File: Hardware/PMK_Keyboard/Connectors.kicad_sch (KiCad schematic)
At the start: 3 parts, among them J101 USB_C_Receptacle_USB2.0

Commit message: Worked on hierachic page again
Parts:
- renumbered J101 to J?
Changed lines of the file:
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@@
+    (stroke (width 0) (type default) (color 0 0 0 0))
+  )
+  (wire (pts (xy 266.7 33.02) (xy 269.24 33.02))
     (stroke (width 0) (type default) (color 0 0 0 0))
   )
@@
     (stroke (width 0) (type default) (color 0 0 0 0))
   )
+  (wire (pts (xy 269.24 36.83) (xy 264.16 36.83))
+    (stroke (width 0) (type default) (color 0 0 0 0))
+  )
   (wire (pts (xy 124.46 93.98) (xy 154.94 93.98))
     (stroke (width 0) (type default) (color 0 0 0 0))
@@
     (stroke (width 0) (type default) (color 0 0 0 0))
   )
+  (wire (pts (xy 264.16 24.13) (xy 264.16 25.4))
+    (stroke (width 0) (type default) (color 0 0 0 0))
+  )
+  (wire (pts (xy 264.16 36.83) (xy 264.16 38.1))
+    (stroke (width 0) (type default) (color 0 0 0 0))
+  )
   (wire (pts (xy 127 106.68) (xy 127 109.22))
     (stroke (width 0) (type default) (color 0 0 0 0))
@@
     (stroke (width 0) (type default) (color 0 0 0 0))
   )
+  (wire (pts (xy 266.7 29.21) (xy 269.24 29.21))
+    (stroke (width 0) (type default) (color 0 0 0 0))
+  )
   (wire (pts (xy 127 104.14) (xy 127 101.6))
     (stroke (width 0) (type default) (color 0 0 0 0))
@@
   )
   (wire (pts (xy 127 86.36) (xy 127 88.9))
+    (stroke (width 0) (type default) (color 0 0 0 0))
+  )
+  (wire (pts (xy 264.16 25.4) (xy 269.24 25.4))
     (stroke (width 0) (type default) (color 0 0 0 0))
   )
@@
     (effects (font (size 1.27 1.27)) (justify left bottom))
   )
-  (global_label "D-" (shape input) (at 129.54 101.6 0) (fields_autoplaced)
+  (global_label "D+" (shape bidirectional) (at 266.7 33.02 180) (fields_autoplaced)
+    (effects (font (size 1.27 1.27)) (justify right))
+    (property "Intersheet References" "${INTERSHEET_REFS}" (id 0) (at 261.4445 32.9406 0)
+      (effects (font (size 1.27 1.27)) (justify right) hide)
+    )
+  )
+  (global_label "D-" (shape bidirectional) (at 129.54 101.6 0) (fields_autoplaced)
     (effects (font (size 1.27 1.27)) (justify left))
     (property "Intersheet References" "${INTERSHEET_REFS}" (id 0) (at 134.7955 101.5206 0)
@@
     )
   )
-  (global_label "D+" (shape input) (at 129.54 106.68 0) (fields_autoplaced)
+  (global_label "D+" (shape bidirectional) (at 129.54 106.68 0) (fields_autoplaced)
     (effects (font (size 1.27 1.27)) (justify left))
     (property "Intersheet References" "${INTERSHEET_REFS}" (id 0) (at 134.7955 106.6006 0)
@@
     )
   )
+  (global_label "D-" (shape bidirectional) (at 266.7 29.21 180) (fields_autoplaced)
+    (effects (font (size 1.27 1.27)) (justify right))
+    (property "Intersheet References" "${INTERSHEET_REFS}" (id 0) (at 261.4445 29.2894 0)
+      (effects (font (size 1.27 1.27)) (justify right) hide)
+    )
+  )
+  (hierarchical_label "D+" (shape bidirectional) (at 269.24 33.02 0)
+    (effects (font (size 1.27 1.27)) (justify left))
+  )
+  (hierarchical_label "GND" (shape passive) (at 269.24 36.83 0)
+    (effects (font (size 1.27 1.27)) (justify left))
+  )
+  (hierarchical_label "VBUS" (shape output) (at 269.24 25.4 0)
+    (effects (font (size 1.27 1.27)) (justify left))
+  )
+  (hierarchical_label "D-" (shape bidirectional) (at 269.24 29.21 0)
+    (effects (font (size 1.27 1.27)) (justify left))
+  )
   (symbol (lib_id "Component lib:R") (at 144.78 99.06 0) (unit 1)
     (in_bom yes) (on_board yes) (fields_autoplaced)
@@
   (symbol (lib_id "power:GND") (at 101.6 129.54 0) (unit 1)
     (in_bom yes) (on_board yes) (fields_autoplaced)
-    (property "Reference" "#PWR084" (id 0) (at 101.6 135.89 0)
+    (property "Reference" "#PWR?" (id 0) (at 101.6 135.89 0)
       (effects (font (size 1.27 1.27)) hide)
     )
@@
   (symbol (lib_id "power:GND") (at 144.78 109.22 0) (unit 1)
     (in_bom yes) (on_board yes) (fields_autoplaced)
-    (property "Reference" "#PWR082" (id 0) (at 144.78 115.57 0)
+    (property "Reference" "#PWR?" (id 0) (at 144.78 115.57 0)
       (effects (font (size 1.27 1.27)) hide)
     )
@@
     (pin "1")
   )
+  (symbol (lib_id "power:VBUS") (at 264.16 24.13 0) (unit 1)
+    (in_bom yes) (on_board yes) (fields_autoplaced)
+    (property "Reference" "#PWR?" (id 0) (at 264.16 27.94 0)
+      (effects (font (size 1.27 1.27)) hide)
+    )
+    (property "Value" "VBUS" (id 1) (at 264.16 20.5542 0))
+    (property "Footprint" "" (id 2) (at 264.16 24.13 0)
+      (effects (font (size 1.27 1.27)) hide)
+    )
+    (property "Datasheet" "" (id 3) (at 264.16 24.13 0)
+      (effects (font (size 1.27 1.27)) hide)
+    )
+    (pin "1")
+  )
   (symbol (lib_id "power:GND") (at 109.22 129.54 0) (unit 1)
     (in_bom yes) (on_board yes) (fields_autoplaced)
-    (property "Reference" "#PWR085" (id 0) (at 109.22 135.89 0)
+    (property "Reference" "#PWR?" (id 0) (at 109.22 135.89 0)
       (effects (font (size 1.27 1.27)) hide)
     )
@@
   (symbol (lib_id "power:GND") (at 154.94 109.22 0) (unit 1)
     (in_bom yes) (on_board yes) (fields_autoplaced)
-    (property "Reference" "#PWR083" (id 0) (at 154.94 115.57 0)
+    (property "Reference" "#PWR?" (id 0) (at 154.94 115.57 0)
       (effects (font (size 1.27 1.27)) hide)
     )
@@
     (pin "2")
   )
+  (symbol (lib_id "power:GND") (at 264.16 38.1 0) (unit 1)
+    (in_bom yes) (on_board yes) (fields_autoplaced)
+    (property "Reference" "#PWR?" (id 0) (at 264.16 44.45 0)
+      (effects (font (size 1.27 1.27)) hide)
+    )
+    (property "Value" "GND" (id 1) (at 264.16 42.5434 0))
+    (property "Footprint" "" (id 2) (at 264.16 38.1 0)
+      (effects (font (size 1.27 1.27)) hide)
+    )
+    (property "Datasheet" "" (id 3) (at 264.16 38.1 0)
+      (effects (font (size 1.27 1.27)) hide)
+    )
+    (pin "1")
+  )
   (symbol (lib_id "power:VBUS") (at 127 86.36 0) (unit 1)
     (in_bom yes) (on_board yes) (fields_autoplaced)
-    (property "Reference" "#PWR081" (id 0) (at 127 90.17 0)
+    (property "Reference" "#PWR?" (id 0) (at 127 90.17 0)
       (effects (font (size 1.27 1.27)) hide)
     )
@@
   (symbol (lib_id "Connector:USB_C_Receptacle_USB2.0") (at 109.22 104.14 0) (unit 1)
     (in_bom yes) (on_board yes) (fields_autoplaced)
-    (property "Reference" "J101" (id 0) (at 109.22 82.6602 0))
+    (property "Reference" "J?" (id 0) (at 109.22 82.6602 0))
     (property "Value" "USB_C_Receptacle_USB2.0" (id 1) (at 109.22 85.1971 0))
     (property "Footprint" "" (id 2) (at 113.03 104.14 0)

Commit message: Worked on hierachic sheet
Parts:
- added J102: Conn_01x02_MountingPin, symbol Connector_Generic_MountingPin:Conn_01x02_MountingPin
- gave numbers to parts that had none: 1
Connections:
- net GND: now also J102.2 (Pin_2), J102.MP (MountPin)
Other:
- moved on the sheet: J101, R101, R102

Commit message: Again on hierachic sheet
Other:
- company: (none) -> PumaCorp
- title: (none) -> PMK_Keyboard
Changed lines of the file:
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@@
 (kicad_sch (version 20211123) (generator eeschema)
   (paper "A4")
+  (title_block
+    (title "PMK_Keyboard")
+    (date "2023-02-06")
+    (rev "HW00")
+    (company "PumaCorp")
+    (comment 1 "Design by: NdG")
+  )
   (junction (at 69.85 68.58) (diameter 0) (color 0 0 0 0)
   )

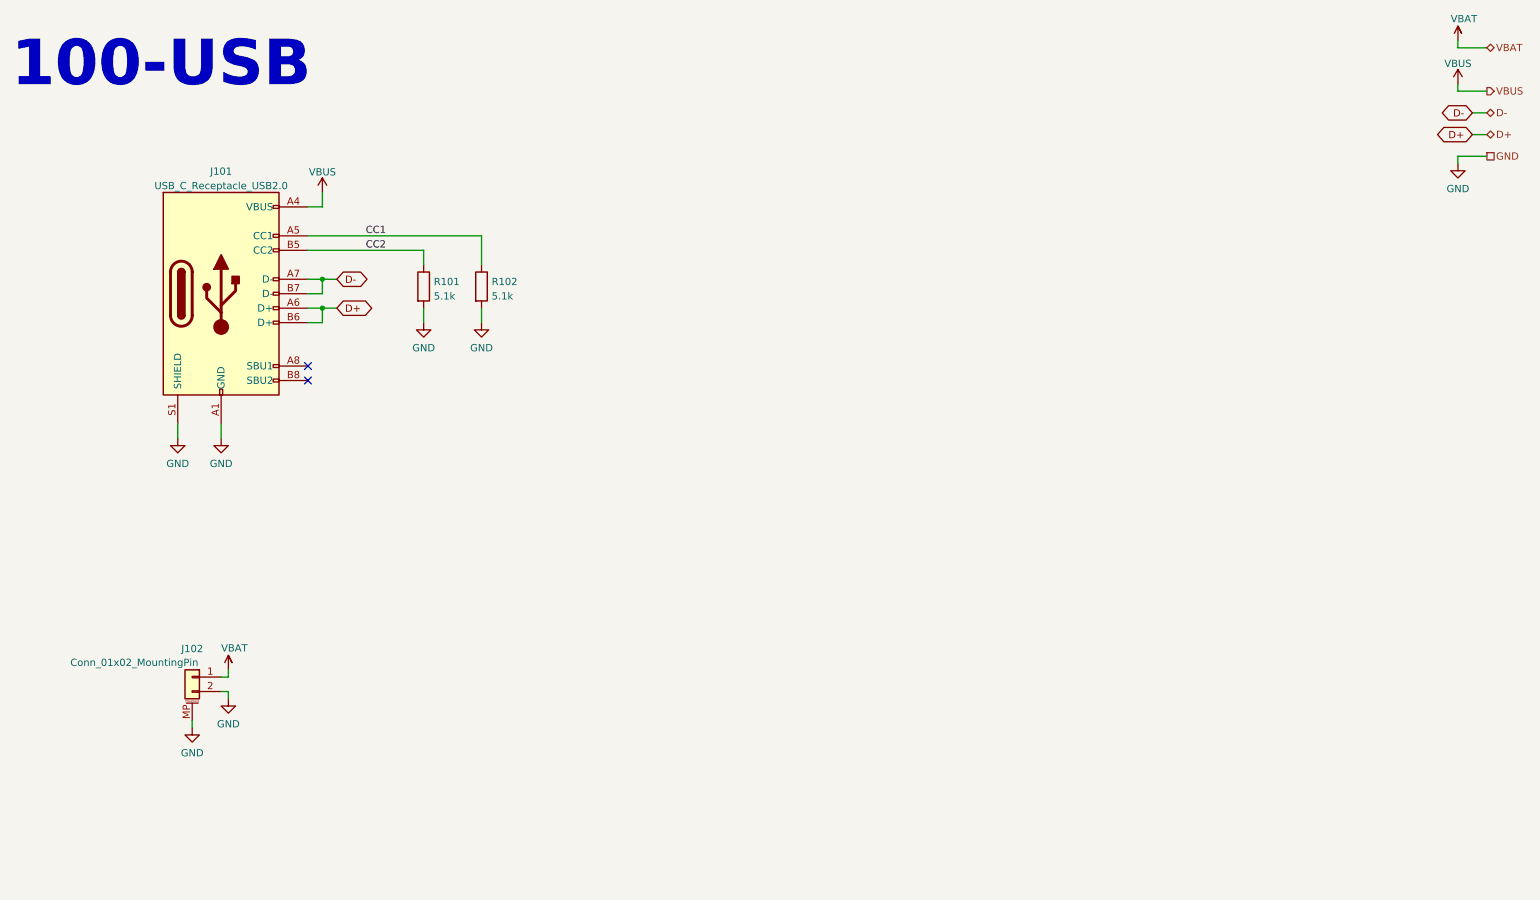
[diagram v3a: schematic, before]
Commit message: Schematic is done, only possible update is change of ESP pins
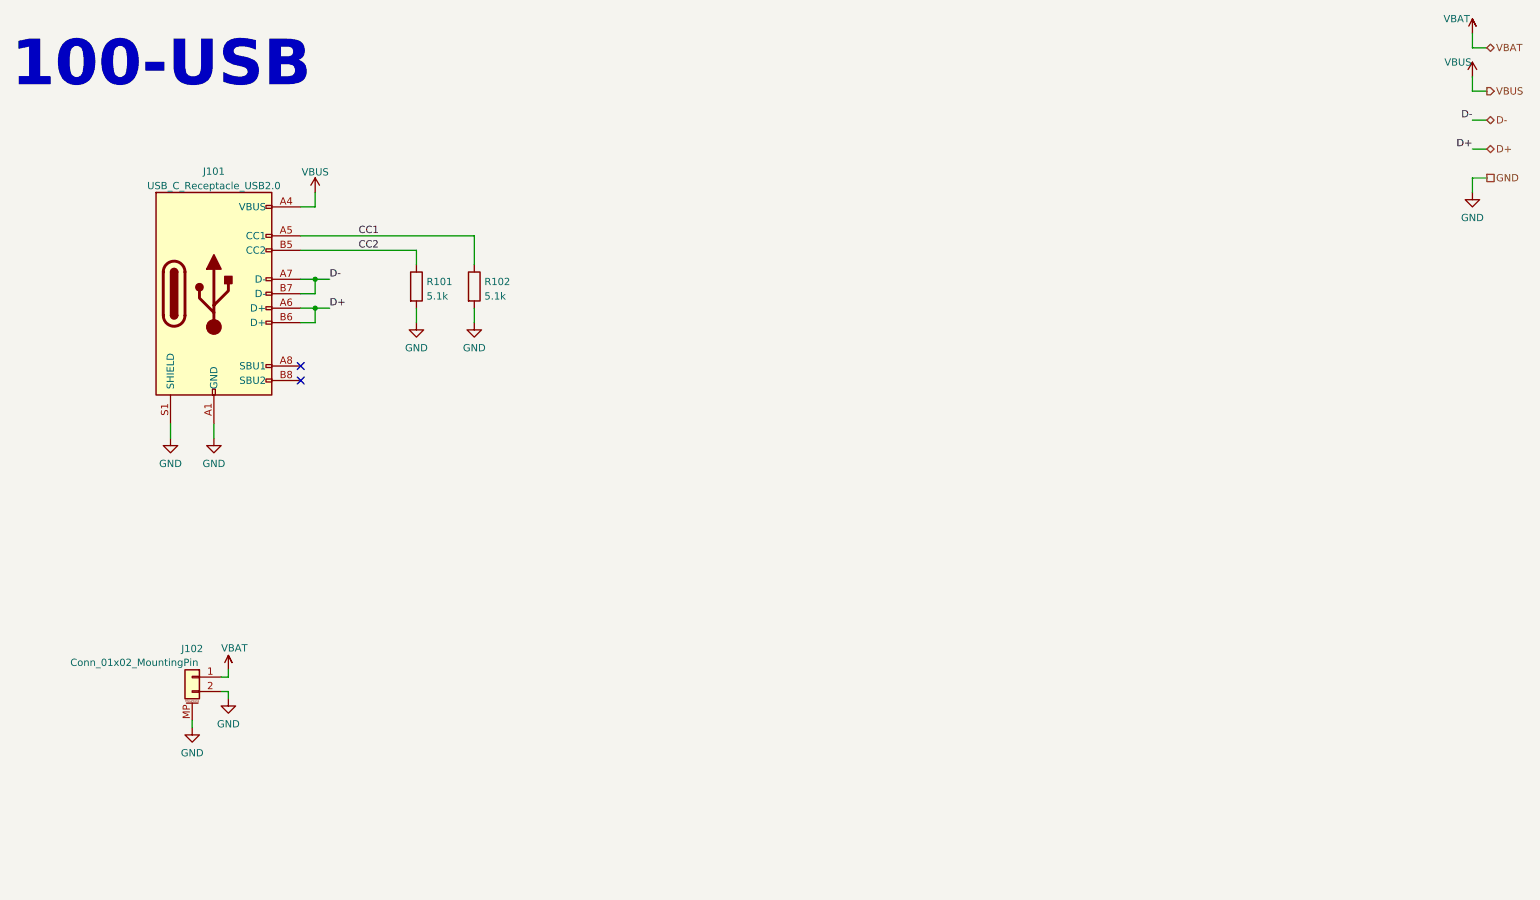
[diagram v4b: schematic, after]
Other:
- moved on the sheet: J101, R101, R102

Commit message: Routing is finally updated
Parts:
- J101: footprint (none) -> Connector_USB:USB_C_Plug_Molex_105444
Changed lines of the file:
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@@
   (symbol (lib_id "Component_lib:VBAT") (at 271.78 20.32 0) (unit 1)
     (in_bom no) (on_board no)
-    (property "Reference" "VBAT0101" (id 0) (at 276.86 15.24 0)
+    (property "Reference" "#VBAT0101" (id 0) (at 276.86 15.24 0)
       (effects (font (size 1.27 1.27)) hide)
     )
@@
   (symbol (lib_id "power:GND") (at 271.78 48.26 0) (unit 1)
     (in_bom yes) (on_board yes) (fields_autoplaced)
-    (property "Reference" "#PWR?" (id 0) (at 271.78 54.61 0)
+    (property "Reference" "#PWR0118" (id 0) (at 271.78 54.61 0)
       (effects (font (size 1.27 1.27)) hide)
     )
@@
   (symbol (lib_id "Component_lib:VBAT") (at 53.34 132.08 0) (unit 1)
     (in_bom no) (on_board no)
-    (property "Reference" "VBAT0102" (id 0) (at 58.42 127 0)
+    (property "Reference" "#VBAT0102" (id 0) (at 58.42 127 0)
       (effects (font (size 1.27 1.27)) hide)
     )
@@
     (property "Reference" "J101" (id 0) (at 50.8 44.5602 0))
     (property "Value" "USB_C_Receptacle_USB2.0" (id 1) (at 50.8 47.0971 0))
-    (property "Footprint" "" (id 2) (at 54.61 66.04 0)
+    (property "Footprint" "Connector_USB:USB_C_Plug_Molex_105444" (id 2) (at 54.61 66.04 0)
       (effects (font (size 1.27 1.27)) hide)
     )

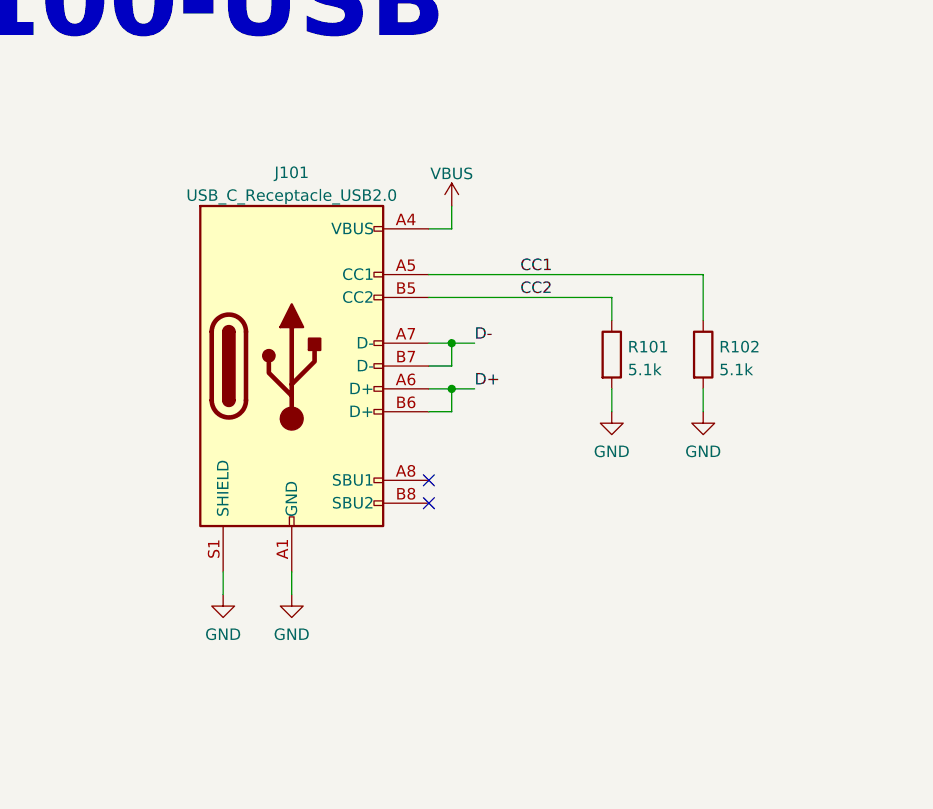
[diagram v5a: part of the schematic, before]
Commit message: Added the correct ref for USB C connector
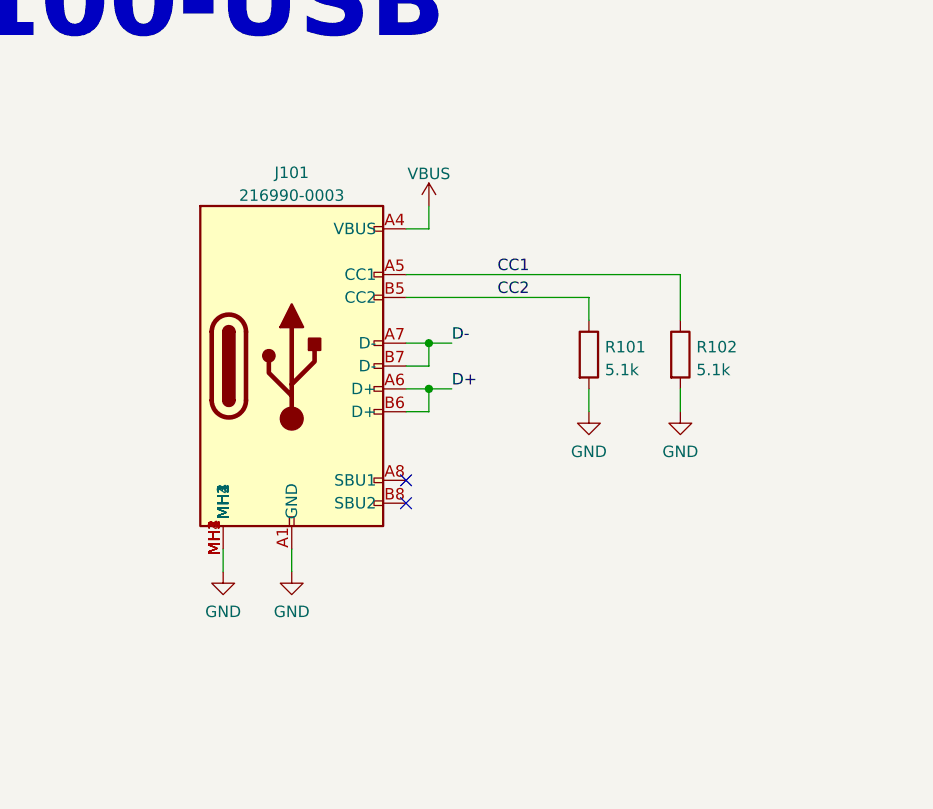
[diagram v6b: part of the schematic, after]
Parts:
- removed J101: USB_C_Receptacle_USB2.0, Connector_USB:USB_C_Plug_Molex_105444, symbol Connector:USB_C_Receptacle_USB2.0
- added J101: 216990-0003, Component_lib:2169900003, symbol Component_lib:216990-0003
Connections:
- net CC1: now also J101.A5 (CC1)
- net CC2: now also J101.B5 (CC2)
- net D+: now also J101.A6 (D+), J101.B6 (D+)
- net D-: now also J101.A7 (D-), J101.B7 (D-)
- net GND: now also J101.A1 (GND), J101.A12 (GND), J101.B1 (GND), J101.B12 (GND), J101.MH1, J101.MH2, J101.MH3, J101.MH4
- net VBUS: now also J101.A4 (VBUS), J101.A9 (VBUS), J101.B4 (VBUS), J101.B9 (VBUS)
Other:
- moved on the sheet: R101, R102

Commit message: Routing is almost done
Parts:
- removed J101: 216990-0003, Component_lib:2169900003, symbol Component_lib:216990-0003
- added J101: USB4510-03-1-A, Component_lib:USB4510031A, symbol Component_lib:USB4510-03-1-A
- J102: footprint (none) -> Component_lib:BatteryHolder_Keystone_1042_1x18650_DUALSIDE
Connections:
- net CC1: now also J101.A5 (CC1)
- net CC2: now also J101.B5 (CC2)
- net D+: now also J101.A6 (D+), J101.B6 (D+)
- net D-: now also J101.A7 (D-), J101.B7 (D-)
- net GND: now also J101.A1 (GND), J101.A12 (GND), J101.B1 (GND), J101.B12 (GND), J101.MH1, J101.MH2, J101.MH3, J101.MH4
- net VBAT: now also J102.1 (Pin_1)
- net VBUS: now also J101.A4 (VBUS), J101.A9 (VBUS), J101.B4 (VBUS), J101.B9 (VBUS)
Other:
- moved on the sheet: J102
